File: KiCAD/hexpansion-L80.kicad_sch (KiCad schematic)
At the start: 22 parts, among them J1 Hexpansion-Connector, J2 Conn_Coaxial, Q1 BC847, U1 L80RE-M37, U2 M24C16-RMN6TP

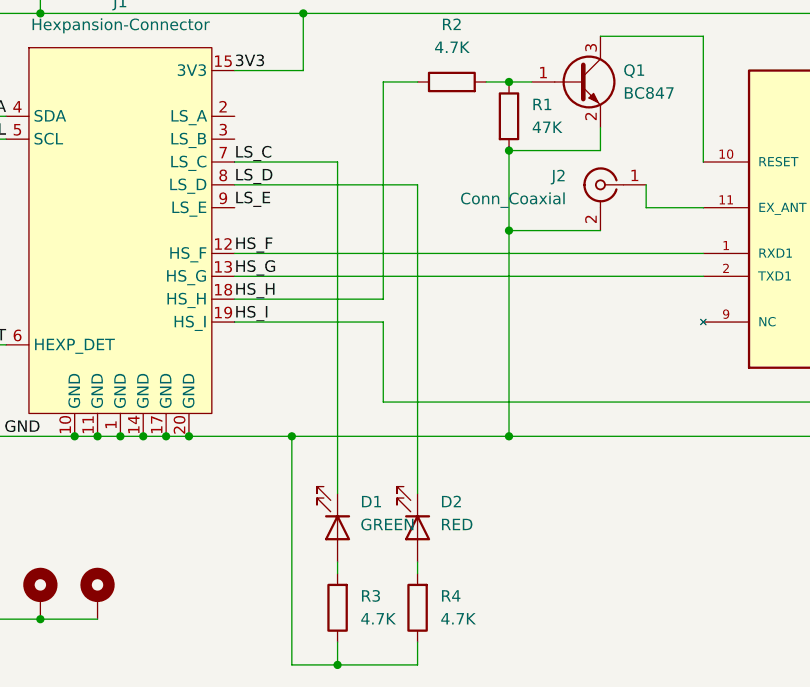
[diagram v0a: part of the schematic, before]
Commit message: rotated LEDs, fixed footprint sizing and regenerated production files
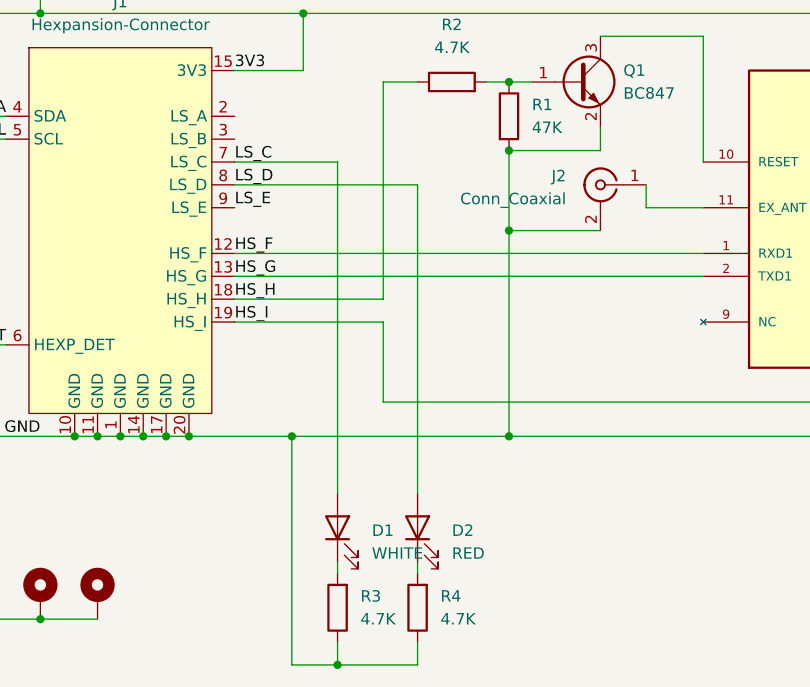
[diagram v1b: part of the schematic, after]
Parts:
- C1, C2, C3: footprint Capacitor_SMD:C_01005_0402Metric -> Capacitor_SMD:C_0402_1005Metric
- D1: value GREEN -> WHITE; footprint LED_SMD:LED_0201_0603Metric -> LED_SMD:LED_0603_1608Metric
- D2: footprint LED_SMD:LED_0201_0603Metric -> LED_SMD:LED_0603_1608Metric
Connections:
- net LS_C: now also D1.2 (A); no longer D1.1 (K)
- net LS_D: now also D2.2 (A); no longer D2.1 (K)
- net at R4.2: now also D2.1 (K); no longer D2.2 (A)
- net at R3.2: now also D1.1 (K); no longer D1.2 (A)
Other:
- moved on the sheet: D1, D2
